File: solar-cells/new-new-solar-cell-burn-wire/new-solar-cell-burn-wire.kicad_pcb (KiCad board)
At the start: 2 copper layers, 80 x 103.5 mm, 27 parts, among them J1 Solar Cell, J2 Burn Wire

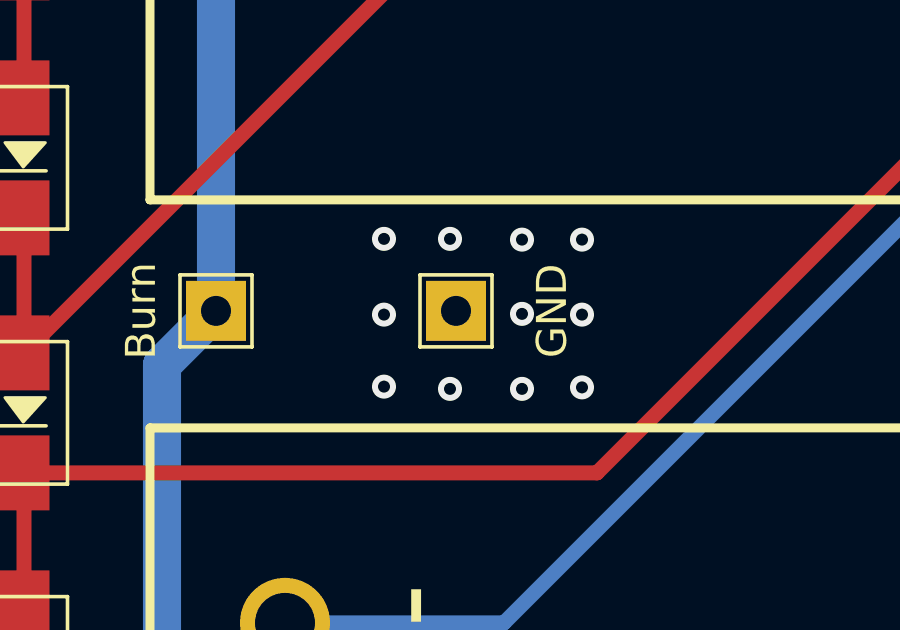
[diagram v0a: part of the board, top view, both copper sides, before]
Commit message: moved GND hole to not interfere w/ chassis beam
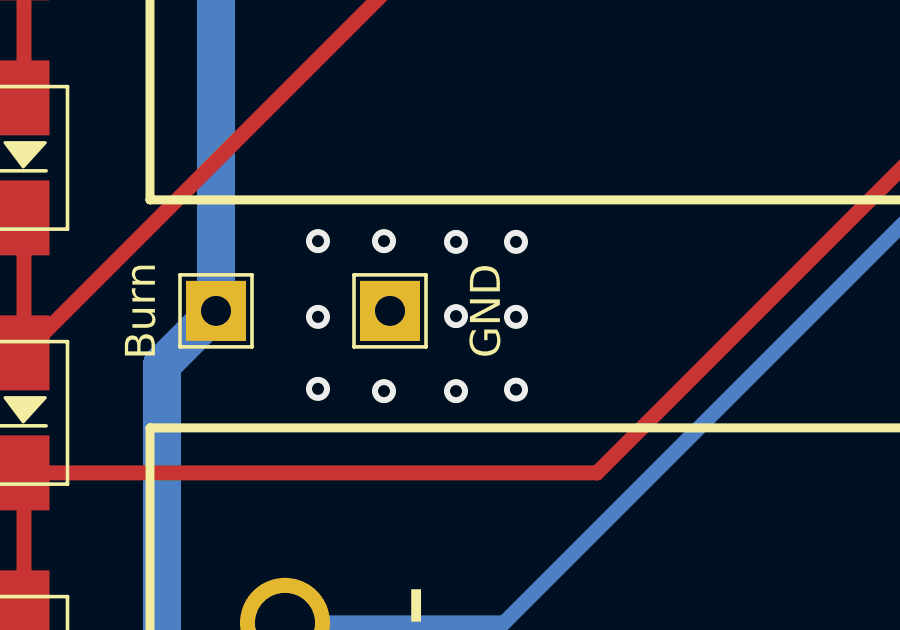
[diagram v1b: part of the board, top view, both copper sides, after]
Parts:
- moved UpperBurn2 2.20 mm to (88.2, 74.6)
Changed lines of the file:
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@@
   )
   (footprint "TestPoint:TestPoint_THTPad_2.0x2.0mm_Drill1.0mm" (layer "F.Cu")
-    (at 90.4 74.6)
+    (at 88.2 74.6)
     (descr "THT rectangular pad as test Point, square 2.0mm_Drill1.0mm  side length, hole diameter 1.0mm")
     (tags "test point THT pad rectangle square")
@@
   )
   (via (at 81.9 128.875) (size 0.8) (drill 0.4) (layers "F.Cu" "B.Cu") (free) (net 1))
-  (via (at 88 77.125) (size 0.8) (drill 0.4) (layers "F.Cu" "B.Cu") (free) (net 1))
+  (via (at 85.8 77.2) (size 0.8) (drill 0.4) (layers "F.Cu" "B.Cu") (free) (net 1))
   (via (at 134.6 106.175) (size 0.8) (drill 0.4) (layers "F.Cu" "B.Cu") (free) (net 1))
   (via (at 136.1 51.9) (size 0.8) (drill 0.4) (layers "F.Cu" "B.Cu") (free) (net 1))
@@
   (via (at 136.6 106.175) (size 0.8) (drill 0.4) (layers "F.Cu" "B.Cu") (free) (net 1))
   (via (at 141.2 103.775) (size 0.8) (drill 0.4) (layers "F.Cu" "B.Cu") (free) (net 1))
-  (via (at 92.6 72.225) (size 0.8) (drill 0.4) (layers "F.Cu" "B.Cu") (free) (net 1))
+  (via (at 90.4 72.3) (size 0.8) (drill 0.4) (layers "F.Cu" "B.Cu") (free) (net 1))
   (via (at 139 108.7) (size 0.8) (drill 0.4) (layers "F.Cu" "B.Cu") (free) (net 1))
-  (via (at 92.6 74.7) (size 0.8) (drill 0.4) (layers "F.Cu" "B.Cu") (free) (net 1))
-  (via (at 88 72.2) (size 0.8) (drill 0.4) (layers "F.Cu" "B.Cu") (free) (net 1))
+  (via (at 90.4 74.775) (size 0.8) (drill 0.4) (layers "F.Cu" "B.Cu") (free) (net 1))
+  (via (at 85.8 72.275) (size 0.8) (drill 0.4) (layers "F.Cu" "B.Cu") (free) (net 1))
   (via (at 83.9 123.9) (size 0.8) (drill 0.4) (layers "F.Cu" "B.Cu") (free) (net 1))
   (via (at 83.9 126.35) (size 0.8) (drill 0.4) (layers "F.Cu" "B.Cu") (free) (net 1))
   (via (at 83.9 128.875) (size 0.8) (drill 0.4) (layers "F.Cu" "B.Cu") (free) (net 1))
-  (via (at 94.6 77.15) (size 0.8) (drill 0.4) (layers "F.Cu" "B.Cu") (free) (net 1))
+  (via (at 92.4 77.225) (size 0.8) (drill 0.4) (layers "F.Cu" "B.Cu") (free) (net 1))
   (via (at 142.7 51.925) (size 0.8) (drill 0.4) (layers "F.Cu" "B.Cu") (free) (net 1))
   (via (at 88.5 123.975) (size 0.8) (drill 0.4) (layers "F.Cu" "B.Cu") (free) (net 1))
   (via (at 134.6 108.675) (size 0.8) (drill 0.4) (layers "F.Cu" "B.Cu") (free) (net 1))
   (via (at 88.5 128.9) (size 0.8) (drill 0.4) (layers "F.Cu" "B.Cu") (free) (net 1))
-  (via (at 90.2 77.2) (size 0.8) (drill 0.4) (layers "F.Cu" "B.Cu") (free) (net 1))
-  (via (at 94.6 72.225) (size 0.8) (drill 0.4) (layers "F.Cu" "B.Cu") (free) (net 1))
+  (via (at 88 77.275) (size 0.8) (drill 0.4) (layers "F.Cu" "B.Cu") (free) (net 1))
+  (via (at 92.4 72.3) (size 0.8) (drill 0.4) (layers "F.Cu" "B.Cu") (free) (net 1))
   (via (at 142.7 56.85) (size 0.8) (drill 0.4) (layers "F.Cu" "B.Cu") (free) (net 1))
   (via (at 141.2 108.7) (size 0.8) (drill 0.4) (layers "F.Cu" "B.Cu") (free) (net 1))
   (via (at 136.6 108.675) (size 0.8) (drill 0.4) (layers "F.Cu" "B.Cu") (free) (net 1))
-  (via (at 94.6 74.725) (size 0.8) (drill 0.4) (layers "F.Cu" "B.Cu") (free) (net 1))
+  (via (at 92.4 74.8) (size 0.8) (drill 0.4) (layers "F.Cu" "B.Cu") (free) (net 1))
   (via (at 141.2 106.2) (size 0.8) (drill 0.4) (layers "F.Cu" "B.Cu") (free) (net 1))
   (via (at 138.3 56.9) (size 0.8) (drill 0.4) (layers "F.Cu" "B.Cu") (free) (net 1))
-  (via (at 92.6 77.2) (size 0.8) (drill 0.4) (layers "F.Cu" "B.Cu") (free) (net 1))
-  (via (at 88 74.725) (size 0.8) (drill 0.4) (layers "F.Cu" "B.Cu") (free) (net 1))
+  (via (at 90.4 77.275) (size 0.8) (drill 0.4) (layers "F.Cu" "B.Cu") (free) (net 1))
+  (via (at 85.8 74.8) (size 0.8) (drill 0.4) (layers "F.Cu" "B.Cu") (free) (net 1))
   (via (at 138.3 51.9) (size 0.8) (drill 0.4) (layers "F.Cu" "B.Cu") (free) (net 1))
   (via (at 140.7 56.9) (size 0.8) (drill 0.4) (layers "F.Cu" "B.Cu") (free) (net 1))
@@
   (via (at 142.7 54.425) (size 0.8) (drill 0.4) (layers "F.Cu" "B.Cu") (free) (net 1))
   (via (at 139 103.7) (size 0.8) (drill 0.4) (layers "F.Cu" "B.Cu") (free) (net 1))
-  (via (at 90.2 72.2) (size 0.8) (drill 0.4) (layers "F.Cu" "B.Cu") (free) (net 1))
+  (via (at 88 72.275) (size 0.8) (drill 0.4) (layers "F.Cu" "B.Cu") (free) (net 1))
   (via (at 140.7 54.425) (size 0.8) (drill 0.4) (layers "F.Cu" "B.Cu") (free) (net 1))
   (via (at 136.1 56.825) (size 0.8) (drill 0.4) (layers "F.Cu" "B.Cu") (free) (net 1))

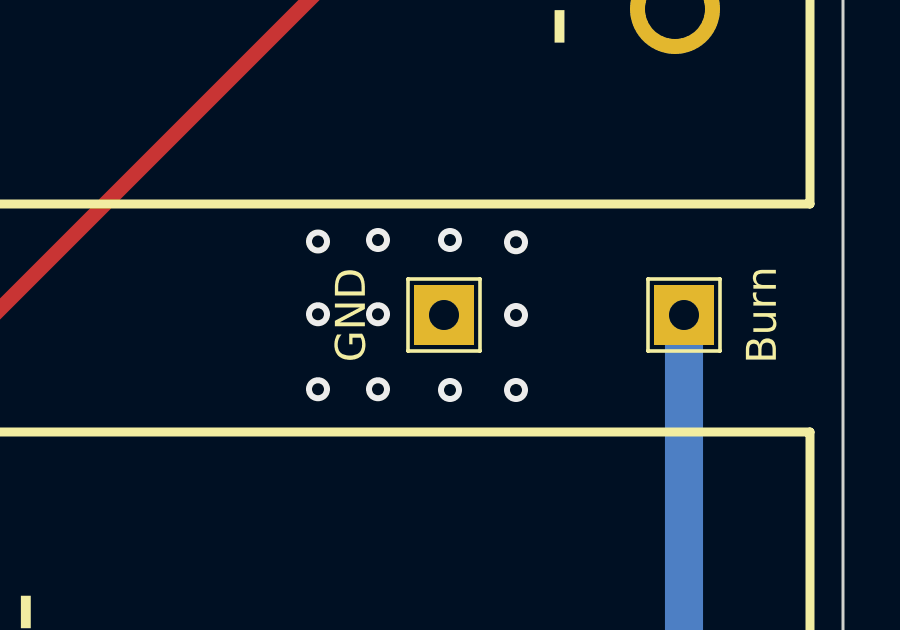
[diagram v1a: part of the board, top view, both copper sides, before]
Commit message: aligned burn wire holes
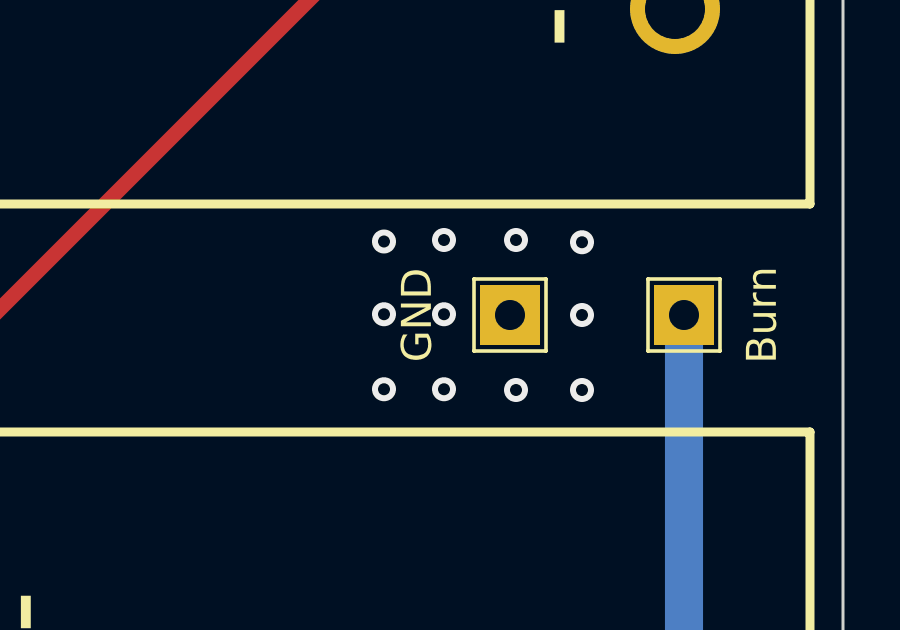
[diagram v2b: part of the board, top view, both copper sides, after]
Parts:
- moved LowerBurn4 2.20 mm to (141.0, 106.2)
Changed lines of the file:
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@@
   )
   (footprint "TestPoint:TestPoint_THTPad_2.0x2.0mm_Drill1.0mm" (layer "F.Cu")
-    (at 138.8 106.2 90)
+    (at 141 106.2 90)
     (descr "THT rectangular pad as test Point, square 2.0mm_Drill1.0mm  side length, hole diameter 1.0mm")
     (tags "test point THT pad rectangle square")
@@
   (via (at 81.9 128.875) (size 0.8) (drill 0.4) (layers "F.Cu" "B.Cu") (free) (net 1))
   (via (at 85.8 77.2) (size 0.8) (drill 0.4) (layers "F.Cu" "B.Cu") (free) (net 1))
-  (via (at 134.6 106.175) (size 0.8) (drill 0.4) (layers "F.Cu" "B.Cu") (free) (net 1))
+  (via (at 136.8 106.175) (size 0.8) (drill 0.4) (layers "F.Cu" "B.Cu") (free) (net 1))
   (via (at 136.1 51.9) (size 0.8) (drill 0.4) (layers "F.Cu" "B.Cu") (free) (net 1))
   (via (at 81.9 123.95) (size 0.8) (drill 0.4) (layers "F.Cu" "B.Cu") (free) (net 1))
   (via (at 140.7 51.925) (size 0.8) (drill 0.4) (layers "F.Cu" "B.Cu") (free) (net 1))
-  (via (at 136.6 106.175) (size 0.8) (drill 0.4) (layers "F.Cu" "B.Cu") (free) (net 1))
-  (via (at 141.2 103.775) (size 0.8) (drill 0.4) (layers "F.Cu" "B.Cu") (free) (net 1))
+  (via (at 138.8 106.175) (size 0.8) (drill 0.4) (layers "F.Cu" "B.Cu") (free) (net 1))
+  (via (at 143.4 103.775) (size 0.8) (drill 0.4) (layers "F.Cu" "B.Cu") (free) (net 1))
   (via (at 90.4 72.3) (size 0.8) (drill 0.4) (layers "F.Cu" "B.Cu") (free) (net 1))
-  (via (at 139 108.7) (size 0.8) (drill 0.4) (layers "F.Cu" "B.Cu") (free) (net 1))
+  (via (at 141.2 108.7) (size 0.8) (drill 0.4) (layers "F.Cu" "B.Cu") (free) (net 1))
   (via (at 90.4 74.775) (size 0.8) (drill 0.4) (layers "F.Cu" "B.Cu") (free) (net 1))
   (via (at 85.8 72.275) (size 0.8) (drill 0.4) (layers "F.Cu" "B.Cu") (free) (net 1))
@@
   (via (at 142.7 51.925) (size 0.8) (drill 0.4) (layers "F.Cu" "B.Cu") (free) (net 1))
   (via (at 88.5 123.975) (size 0.8) (drill 0.4) (layers "F.Cu" "B.Cu") (free) (net 1))
-  (via (at 134.6 108.675) (size 0.8) (drill 0.4) (layers "F.Cu" "B.Cu") (free) (net 1))
+  (via (at 136.8 108.675) (size 0.8) (drill 0.4) (layers "F.Cu" "B.Cu") (free) (net 1))
   (via (at 88.5 128.9) (size 0.8) (drill 0.4) (layers "F.Cu" "B.Cu") (free) (net 1))
   (via (at 88 77.275) (size 0.8) (drill 0.4) (layers "F.Cu" "B.Cu") (free) (net 1))
   (via (at 92.4 72.3) (size 0.8) (drill 0.4) (layers "F.Cu" "B.Cu") (free) (net 1))
   (via (at 142.7 56.85) (size 0.8) (drill 0.4) (layers "F.Cu" "B.Cu") (free) (net 1))
-  (via (at 141.2 108.7) (size 0.8) (drill 0.4) (layers "F.Cu" "B.Cu") (free) (net 1))
-  (via (at 136.6 108.675) (size 0.8) (drill 0.4) (layers "F.Cu" "B.Cu") (free) (net 1))
+  (via (at 143.4 108.7) (size 0.8) (drill 0.4) (layers "F.Cu" "B.Cu") (free) (net 1))
+  (via (at 138.8 108.675) (size 0.8) (drill 0.4) (layers "F.Cu" "B.Cu") (free) (net 1))
   (via (at 92.4 74.8) (size 0.8) (drill 0.4) (layers "F.Cu" "B.Cu") (free) (net 1))
-  (via (at 141.2 106.2) (size 0.8) (drill 0.4) (layers "F.Cu" "B.Cu") (free) (net 1))
+  (via (at 143.4 106.2) (size 0.8) (drill 0.4) (layers "F.Cu" "B.Cu") (free) (net 1))
   (via (at 138.3 56.9) (size 0.8) (drill 0.4) (layers "F.Cu" "B.Cu") (free) (net 1))
   (via (at 90.4 77.275) (size 0.8) (drill 0.4) (layers "F.Cu" "B.Cu") (free) (net 1))
@@
   (via (at 138.3 51.9) (size 0.8) (drill 0.4) (layers "F.Cu" "B.Cu") (free) (net 1))
   (via (at 140.7 56.9) (size 0.8) (drill 0.4) (layers "F.Cu" "B.Cu") (free) (net 1))
-  (via (at 134.6 103.75) (size 0.8) (drill 0.4) (layers "F.Cu" "B.Cu") (free) (net 1))
-  (via (at 136.6 103.7) (size 0.8) (drill 0.4) (layers "F.Cu" "B.Cu") (free) (net 1))
+  (via (at 136.8 103.75) (size 0.8) (drill 0.4) (layers "F.Cu" "B.Cu") (free) (net 1))
+  (via (at 138.8 103.7) (size 0.8) (drill 0.4) (layers "F.Cu" "B.Cu") (free) (net 1))
   (via (at 81.9 126.375) (size 0.8) (drill 0.4) (layers "F.Cu" "B.Cu") (free) (net 1))
   (via (at 86.3 128.9) (size 0.8) (drill 0.4) (layers "F.Cu" "B.Cu") (free) (net 1))
   (via (at 86.3 123.9) (size 0.8) (drill 0.4) (layers "F.Cu" "B.Cu") (free) (net 1))
   (via (at 142.7 54.425) (size 0.8) (drill 0.4) (layers "F.Cu" "B.Cu") (free) (net 1))
-  (via (at 139 103.7) (size 0.8) (drill 0.4) (layers "F.Cu" "B.Cu") (free) (net 1))
+  (via (at 141.2 103.7) (size 0.8) (drill 0.4) (layers "F.Cu" "B.Cu") (free) (net 1))
   (via (at 88 72.275) (size 0.8) (drill 0.4) (layers "F.Cu" "B.Cu") (free) (net 1))
   (via (at 140.7 54.425) (size 0.8) (drill 0.4) (layers "F.Cu" "B.Cu") (free) (net 1))

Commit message: changed burn wire to 3s2p config
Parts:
- removed D3, D4, D5, D6, D9: CDBA240LL-HF, ISP:DO-214AC
- moved D2 45.8 mm to (120.4, 106.2), turned to 0 degrees
- moved D1 11.1 mm to (76.1, 114.6), turned to -90 degrees
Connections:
- D1 pad 1: Net-(D1-Pad1) -> VSOLAR
- D2 pad 1: Net-(D1-Pad2) -> VSOLAR
- SC1 pad 1: Net-(D1-Pad1) -> Net-(D1-Pad2)
- SC1 pad 2: Net-(D1-Pad2) -> Net-(SC1-Pad2)
- SC2 pad 1: Net-(D1-Pad2) -> Net-(SC1-Pad2)
- SC2 pad 2: Net-(D2-Pad2) -> Net-(SC2-Pad2)
- SC3 pad 1: Net-(D2-Pad2) -> Net-(SC2-Pad2)
- SC3 pad 2: Net-(D3-Pad2) -> GND
- SC4 pad 1: Net-(D3-Pad2) -> Net-(D2-Pad2)
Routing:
- net Net-(D3-Pad2): track 110.9 -> 0.00 mm
- net Net-(SC4-Pad2): track 134.8 -> 40.4 mm
- net Net-(SC5-Pad2): track 115.0 -> 34.3 mm
- net Net-(SC2-Pad2): track 0.00 -> 43.5 mm
- net Net-(D2-Pad2): track 59.3 -> 23.1 mm
- net VSOLAR: track 32.4 -> 53.3 mm
- net Net-(D1-Pad2): track 25.7 -> 8.60 mm
- net Net-(D1-Pad1): track 15.9 -> 0.00 mm
- net Net-(SC1-Pad2): track 0.00 -> 13.6 mm
